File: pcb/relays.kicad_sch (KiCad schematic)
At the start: 17 parts, among them J5 HEATER OUT, J6 HUMIDIFIER OUT, K1 SANYOU_SRD_Form_C, Q2 IRLZ44N, Q3 NPN, U5 SFH617A-1X001

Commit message: fixed capactior, inductor and, voltage ic footprint in schematic; added missing labels on the pcb; clarified and added missing items in the BOM
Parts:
- C6: footprint Capacitor_THT:CP_Radial_D8.0mm_P3.50mm -> Capacitor_THT:CP_Radial_D12.5mm_P5.00mm
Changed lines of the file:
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@@
 			)
 		)
-		(property "Footprint" "Capacitor_THT:CP_Radial_D8.0mm_P3.50mm"
+		(property "Footprint" "Capacitor_THT:CP_Radial_D12.5mm_P5.00mm"
 			(at 79.7052 104.14 0)
 			(effects

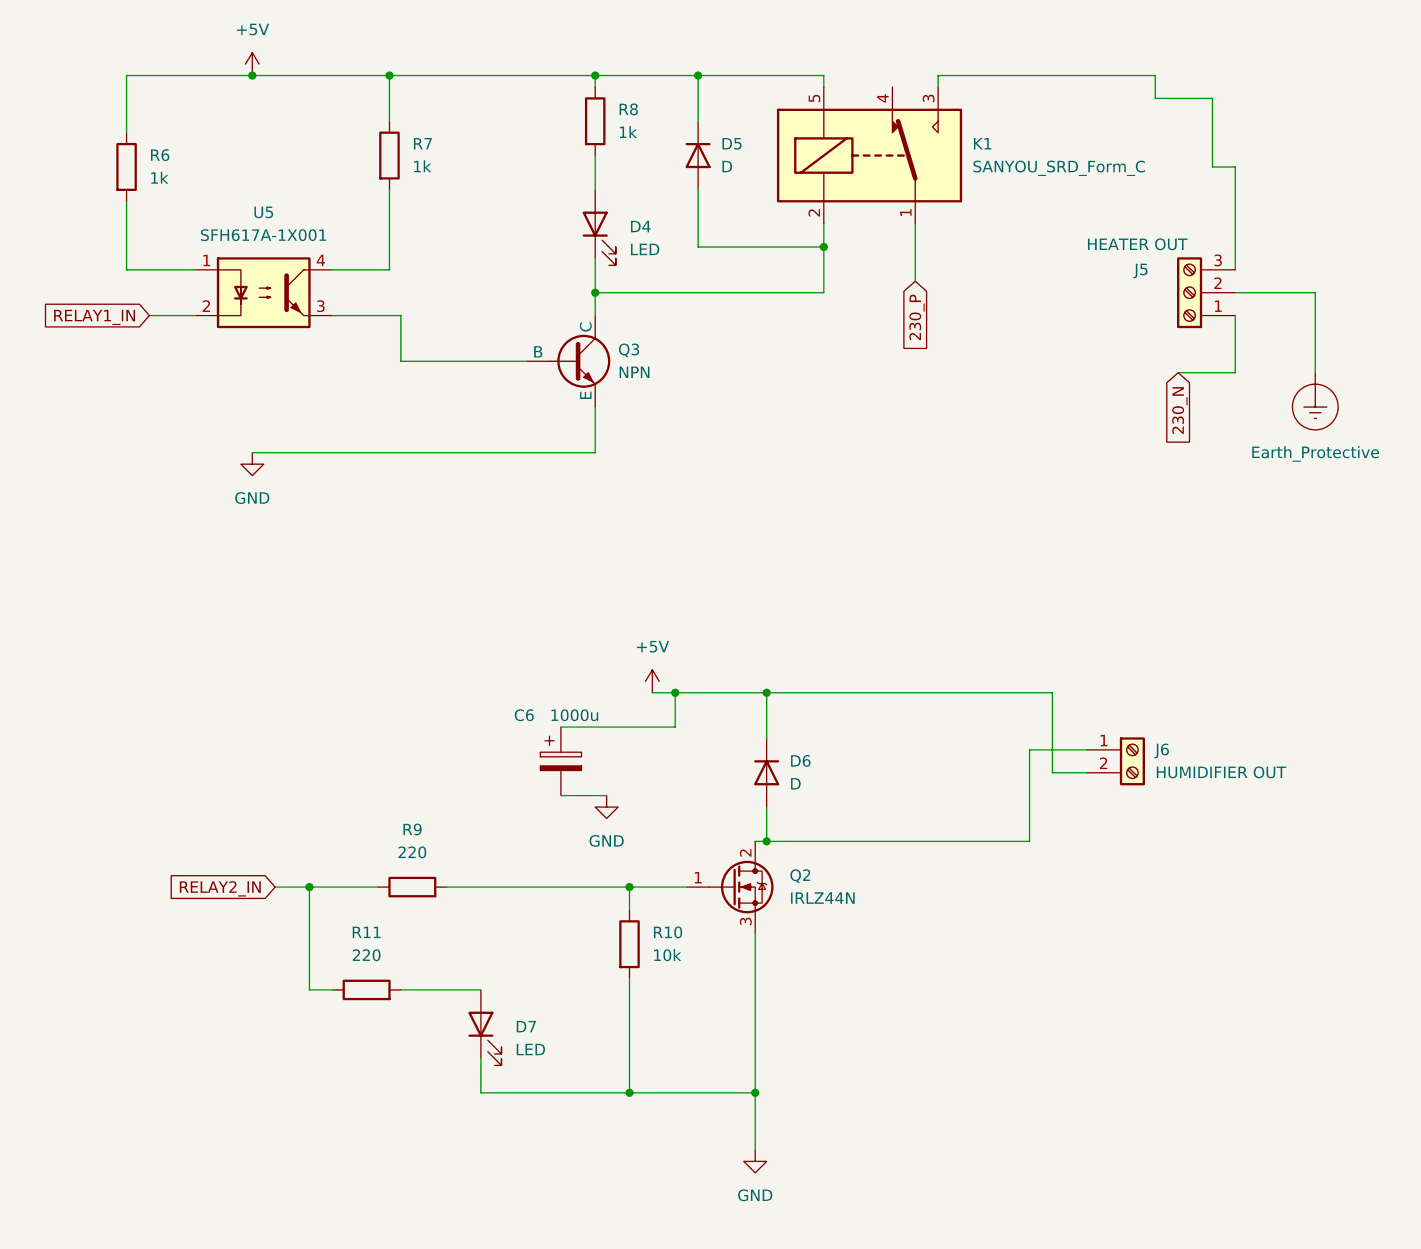
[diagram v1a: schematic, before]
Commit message: changed esp board to nodemcu 32s, limited current on leds, added diode for 5v usb programming backfeed, made switched labels more clear, fixed dallas data bus pull up, added pcb holes for mounting, removed unnecessary BOM items, removed relay optocoupler, re-routed pcb, fixed TODOs, added new render
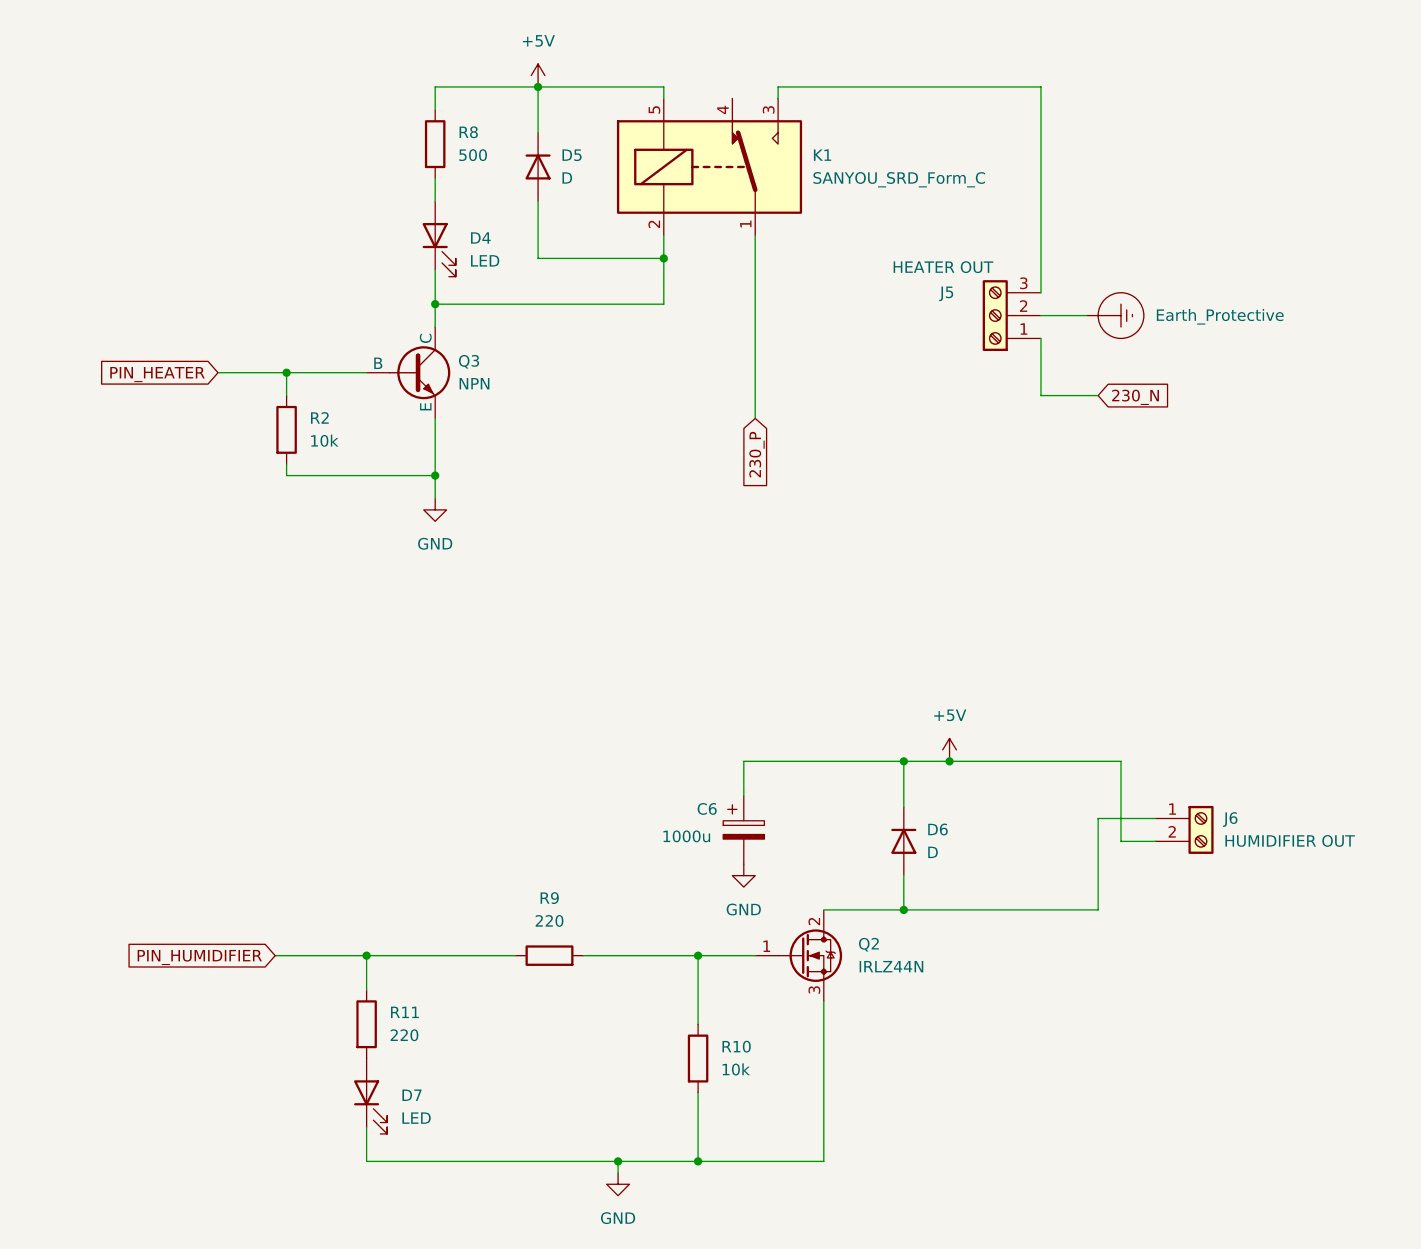
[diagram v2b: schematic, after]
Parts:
- removed R6, R7: 1k, Resistor_THT:R_Axial_DIN0411_L9.9mm_D3.6mm_P12.70mm_Horizontal, symbol Device:R
- removed U5: SFH617A-1X001, Package_DIP:DIP-4_W7.62mm, symbol Isolator:SFH617A-1X001
- added R2: 10k, symbol Device:R
- R8: value 1k -> 500
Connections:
- net GND: now also R2.2
- net PIN_HEATER: now reaches Q3.2 (B)
- net PIN_HEATER: now also R2.1
- net RELAY2_IN renamed PIN_HUMIDIFIER
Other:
- moved on the sheet: C6, D4, D5, D6, D7, J5, J6, K1, Q2, Q3, R10, R11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
